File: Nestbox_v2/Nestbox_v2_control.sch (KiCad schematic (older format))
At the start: 28 parts, among them CON301 Micro_SD_Card, P301 RX/TX, P302 TST/RST, P303 DEBUG_3V3, SW301 SMD-BUTTON_2P-3.0X2.5X1.2+0.4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, U301 MSP430FR5969, Y301 Crystal

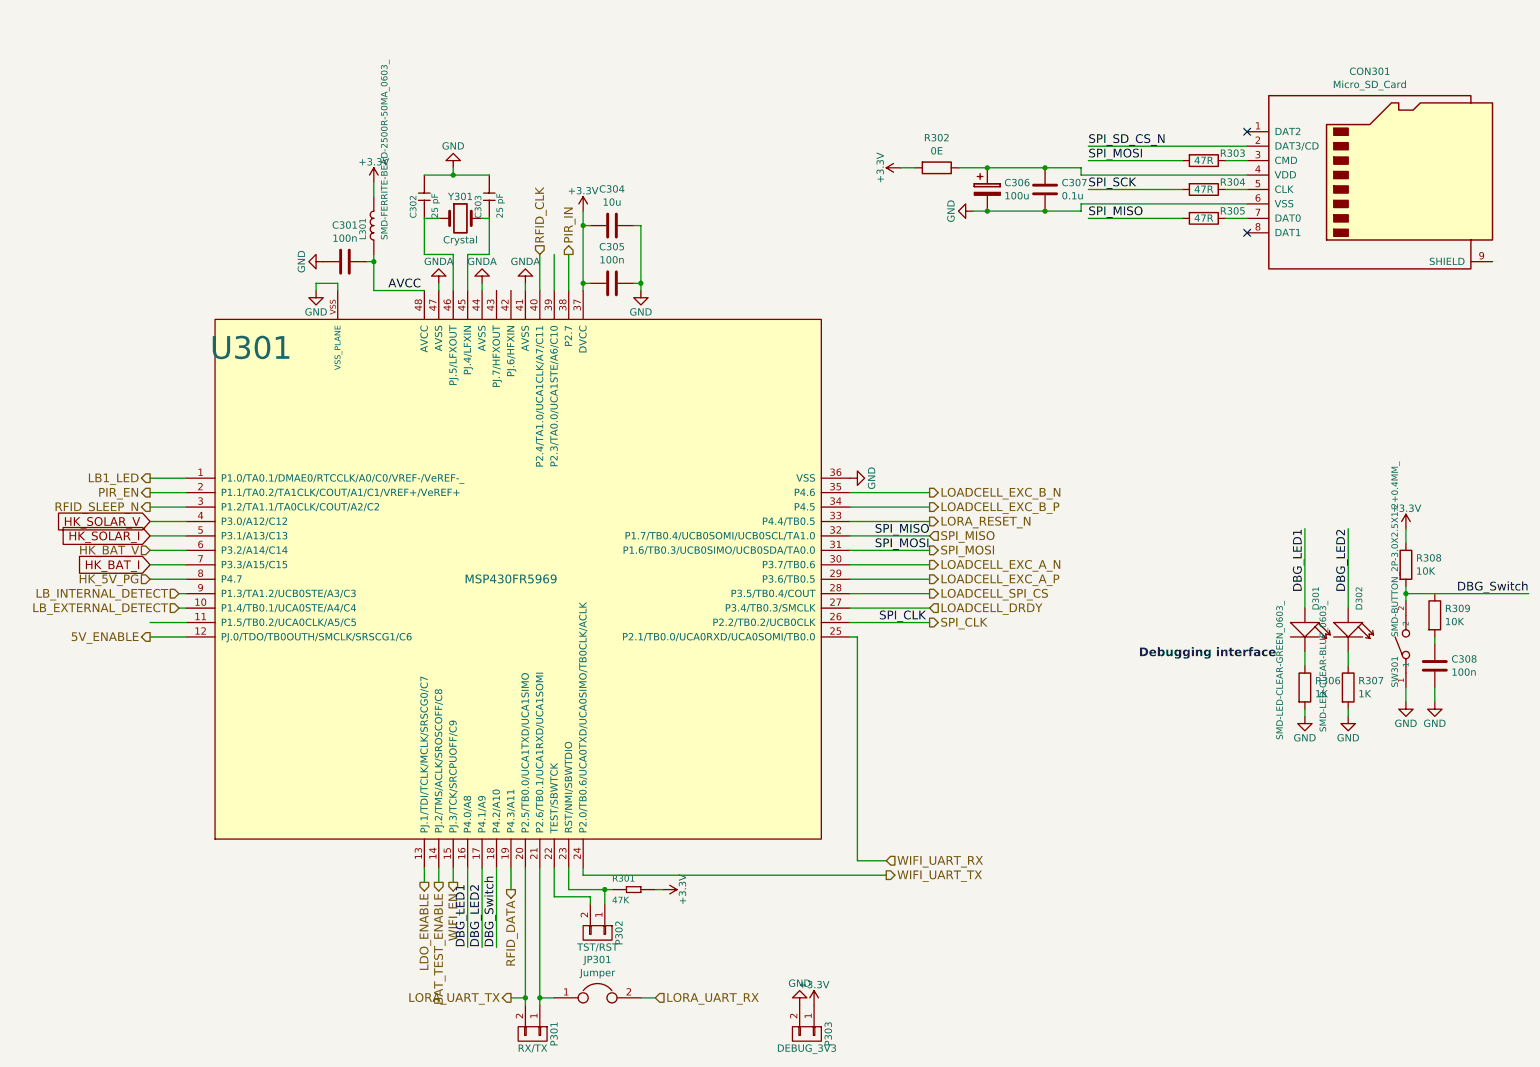
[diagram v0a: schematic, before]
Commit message: all footprints assigned except mosfets; final connectors and their locatino, started component placement
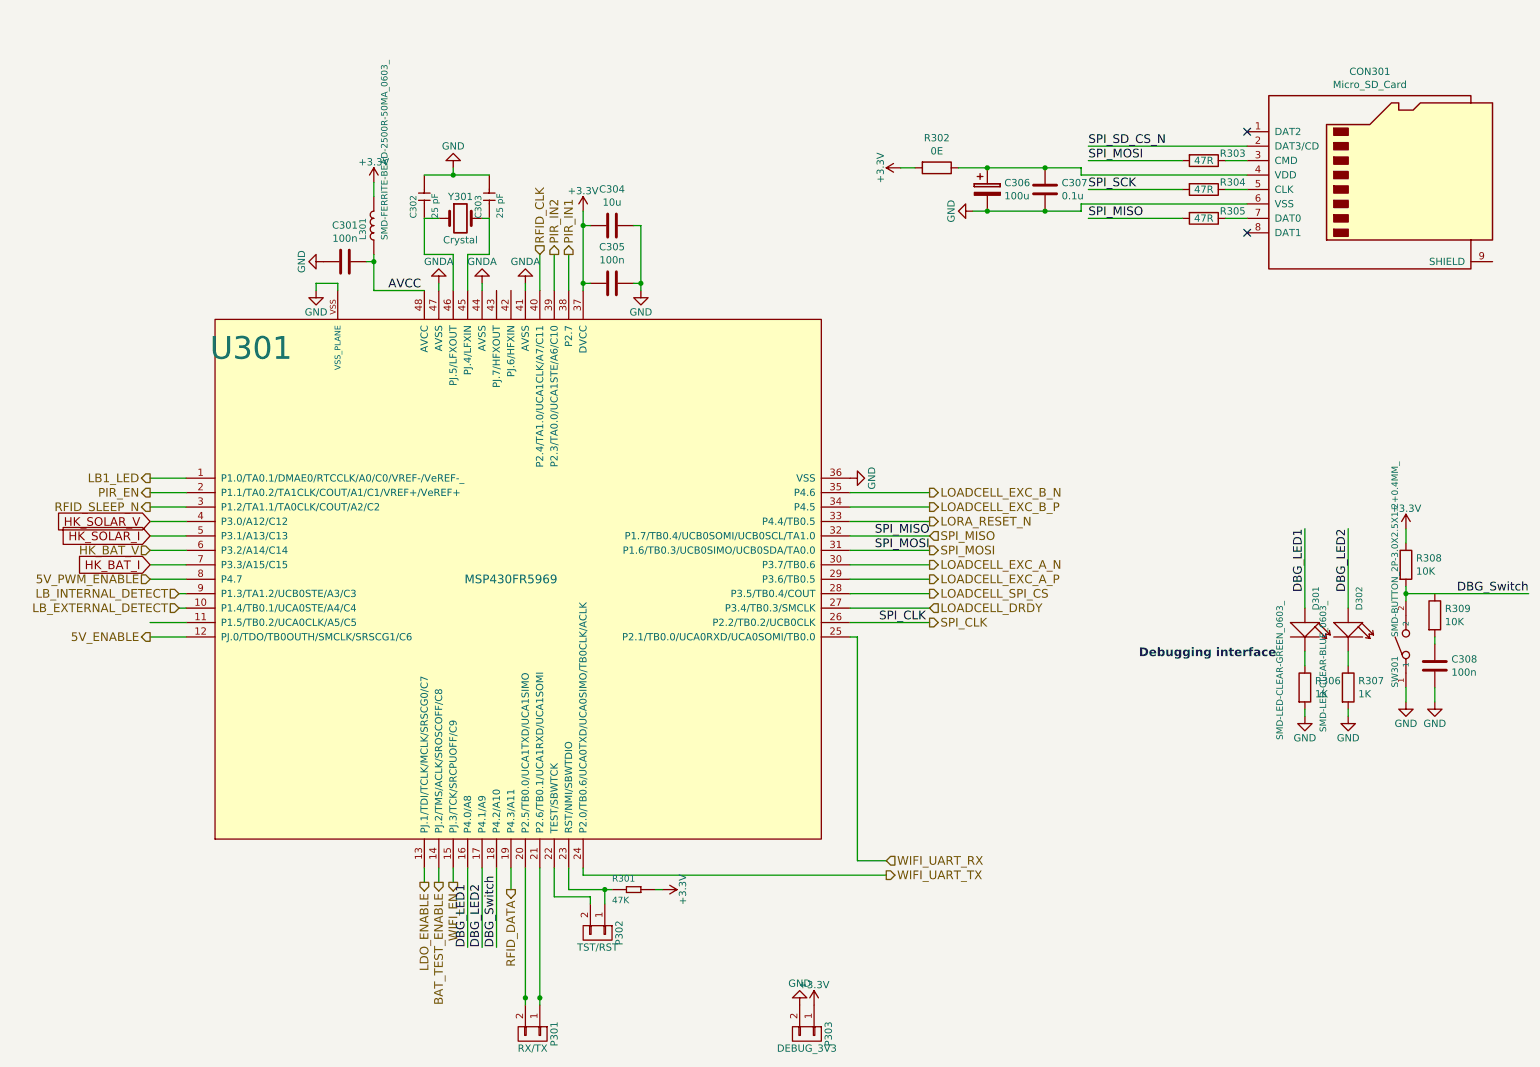
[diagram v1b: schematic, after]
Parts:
- removed JP301: Jumper, Pin_Headers:Pin_Header_Straight_1x02, symbol Jumper
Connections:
- net PIR_IN2: now reaches U301.39 (P2.3/TA0.0/UCA1STE/A6/C10)
- net HK_5V_PG renamed 5V_PWM_ENABLE
- net LORA_UART_TX: no longer names the net of P301.2 (P2), U301.20 (P2.5/TB0.0/UCA1TXD/UCA1SIMO)
- net PIR_IN renamed PIR_IN1
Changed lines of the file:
@@
 EESchema Schematic File Version 2
-LIBS:Nestbox_v2-rescue
-LIBS:Octanis3
 LIBS:power
 LIBS:device
-LIBS:switches
-LIBS:relays
-LIBS:motors
 LIBS:transistors
 LIBS:conn
@@
 LIBS:contrib
 LIBS:valves
-LIBS:SeeedOPL-Capacitor-2016
-LIBS:SeeedOPL-Connector-2016
-LIBS:SeeedOPL-Crystal Oscillator-2016
-LIBS:SeeedOPL-Diode-2016
-LIBS:SeeedOPL-Display-2016
-LIBS:SeeedOPL-Fuse-2016
-LIBS:SeeedOPL-IC-2016
-LIBS:SeeedOPL-Inductor-2016
-LIBS:SeeedOPL-LED-2016
-LIBS:SeeedOPL-Relay-2016
-LIBS:SeeedOPL-Resistor-2016
-LIBS:SeeedOPL-Sensor-2016
-LIBS:SeeedOPL-Switch-2016
-LIBS:SeeedOPL-Transistor-2016
+LIBS:Octanis3
 LIBS:Nestbox_v2-cache
 EELAYER 25 0
@@
 $EndComp
 $Comp
-L GND #PWR313
+L GND #PWR022
 U 1 1 586416A7
 P 6150 3750
-F 0 "#PWR313" H 6150 3500 50  0001 C CNN
+F 0 "#PWR022" H 6150 3500 50  0001 C CNN
 F 1 "GND" H 6150 3600 50  0000 C CNN
 F 2 "" H 6150 3750 50  0000 C CNN
@@
 $EndComp
 $Comp
-L +3.3V #PWR308
+L +3.3V #PWR023
 U 1 1 586418DC
 P 4300 1900
-F 0 "#PWR308" H 4300 1750 50  0001 C CNN
+F 0 "#PWR023" H 4300 1750 50  0001 C CNN
 F 1 "+3.3V" H 4300 2040 50  0000 C CNN
 F 2 "" H 4300 1900 50  0000 C CNN
@@
 $EndComp
 $Comp
-L GND #PWR302
+L GND #PWR024
 U 1 1 58641ADD
 P 2500 2250
-F 0 "#PWR302" H 2500 2000 50  0001 C CNN
+F 0 "#PWR024" H 2500 2000 50  0001 C CNN
 F 1 "GND" H 2500 2100 50  0000 C CNN
 F 2 "" H 2500 2250 50  0000 C CNN
@@
 $EndComp
 $Comp
-L +3.3V #PWR303
+L +3.3V #PWR025
 U 1 1 58641B00
 P 2850 1700
-F 0 "#PWR303" H 2850 1550 50  0001 C CNN
+F 0 "#PWR025" H 2850 1550 50  0001 C CNN
 F 1 "+3.3V" H 2850 1840 50  0000 C CNN
 F 2 "" H 2850 1700 50  0000 C CNN
@@
 $EndComp
 $Comp
-L GND #PWR309
+L GND #PWR026
 U 1 1 58652F3A
 P 4700 2450
-F 0 "#PWR309" H 4700 2200 50  0001 C CNN
+F 0 "#PWR026" H 4700 2200 50  0001 C CNN
 F 1 "GND" H 4700 2300 50  0000 C CNN
 F 2 "" H 4700 2450 50  0000 C CNN
@@
 $EndComp
 $Comp
-L GND #PWR305
+L GND #PWR027
 U 1 1 5865358A
 P 3400 1600
-F 0 "#PWR305" H 3400 1350 50  0001 C CNN
+F 0 "#PWR027" H 3400 1350 50  0001 C CNN
 F 1 "GND" H 3400 1450 50  0000 C CNN
 F 2 "" H 3400 1600 50  0000 C CNN
@@
 $EndComp
 $Comp
-L GNDA #PWR304
+L GNDA #PWR028
 U 1 1 587B6902
 P 3300 2400
-F 0 "#PWR304" H 3300 2150 50  0001 C CNN
+F 0 "#PWR028" H 3300 2150 50  0001 C CNN
 F 1 "GNDA" H 3300 2250 50  0000 C CNN
 F 2 "" H 3300 2400 50  0000 C CNN
@@
 $EndComp
 $Comp
-L GNDA #PWR306
+L GNDA #PWR029
 U 1 1 587B69F1
 P 3600 2400
-F 0 "#PWR306" H 3600 2150 50  0001 C CNN
+F 0 "#PWR029" H 3600 2150 50  0001 C CNN
 F 1 "GNDA" H 3600 2250 50  0000 C CNN
 F 2 "" H 3600 2400 50  0000 C CNN
@@
 $EndComp
 $Comp
-L GNDA #PWR307
+L GNDA #PWR030
 U 1 1 587B6A2F
 P 3900 2400
-F 0 "#PWR307" H 3900 2150 50  0001 C CNN
+F 0 "#PWR030" H 3900 2150 50  0001 C CNN
 F 1 "GNDA" H 3900 2250 50  0000 C CNN
 F 2 "" H 3900 2400 50  0000 C CNN
@@
 $EndComp
 $Comp
-L GND #PWR319
+L GND #PWR031
 U 1 1 587B96DD
 P 10000 5300
-F 0 "#PWR319" H 10000 5050 50  0001 C CNN
+F 0 "#PWR031" H 10000 5050 50  0001 C CNN
 F 1 "GND" H 10000 5150 50  0000 C CNN
 F 2 "" H 10000 5300 50  0000 C CNN
@@
 $EndComp
 $Comp
-L +3.3V #PWR318
+L +3.3V #PWR032
 U 1 1 587B9736
 P 10000 4100
-F 0 "#PWR318" H 10000 3950 50  0001 C CNN
+F 0 "#PWR032" H 10000 3950 50  0001 C CNN
 F 1 "+3.3V" H 10000 4240 50  0000 C CNN
 F 2 "" H 10000 4100 50  0000 C CNN
@@
 $EndComp
 $Comp
-L GND #PWR317
+L GND #PWR033
 U 1 1 587B97E4
 P 9600 5400
-F 0 "#PWR317" H 9600 5150 50  0001 C CNN
+F 0 "#PWR033" H 9600 5150 50  0001 C CNN
 F 1 "GND" H 9600 5250 50  0000 C CNN
 F 2 "" H 9600 5400 50  0000 C CNN
@@
 $EndComp
 $Comp
-L GND #PWR316
+L GND #PWR034
 U 1 1 587B9834
 P 9300 5400
-F 0 "#PWR316" H 9300 5150 50  0001 C CNN
+F 0 "#PWR034" H 9300 5150 50  0001 C CNN
 F 1 "GND" H 9300 5250 50  0000 C CNN
 F 2 "" H 9300 5400 50  0000 C CNN
@@
 	9300 4950 9300 5050
 $Comp
-L GND #PWR301
+L GND #PWR035
 U 1 1 587D2523
 P 2450 2450
-F 0 "#PWR301" H 2450 2200 50  0001 C CNN
+F 0 "#PWR035" H 2450 2200 50  0001 C CNN
 F 1 "GND" H 2450 2300 50  0000 C CNN
 F 2 "" H 2450 2450 50  0000 C CNN
@@
 	4350 6650 4350 6700
 $Comp
-L +3.3V #PWR310
+L +3.3V #PWR036
 U 1 1 58BC4BB7
 P 4850 6600
-F 0 "#PWR310" H 4850 6450 50  0001 C CNN
+F 0 "#PWR036" H 4850 6450 50  0001 C CNN
 F 1 "+3.3V" H 4850 6740 50  0000 C CNN
 F 2 "" H 4850 6600 50  0000 C CNN
@@
 	10200 4850 10200 4900
 $Comp
-L GND #PWR320
+L GND #PWR037
 U 1 1 58BF19D6
 P 10200 5300
-F 0 "#PWR320" H 10200 5050 50  0001 C CNN
+F 0 "#PWR037" H 10200 5050 50  0001 C CNN
 F 1 "GND" H 10200 5150 50  0000 C CNN
 F 2 "" H 10200 5300 50  0000 C CNN
@@
 SPI_MOSI
 $Comp
-L +3.3V #PWR314
+L +3.3V #PWR038
 U 1 1 59FCECA7
 P 6500 1600
-F 0 "#PWR314" H 6500 1450 50  0001 C CNN
+F 0 "#PWR038" H 6500 1450 50  0001 C CNN
 F 1 "+3.3V" H 6500 1740 50  0000 C CNN
 F 2 "" H 6500 1600 50  0000 C CNN
@@
 $EndComp
 $Comp
-L GND #PWR315
+L GND #PWR039
 U 1 1 59FCED84
 P 7000 1900
-F 0 "#PWR315" H 7000 1650 50  0001 C CNN
+F 0 "#PWR039" H 7000 1650 50  0001 C CNN
 F 1 "GND" H 7000 1750 50  0000 C CNN
 F 2 "" H 7000 1900 50  0000 C CNN
@@
 Wire Wire Line
 	1550 4050 1300 4050
-Wire Wire Line
-	4800 7350 4700 7350
-$Comp
-L Jumper JP301
-U 1 1 5A03190F
-P 4400 7350
-F 0 "JP301" H 4400 7614 50  0000 C CNN
-F 1 "Jumper" H 4400 7523 50  0000 C CNN
-F 2 "Pin_Headers:Pin_Header_Straight_1x02" H 4400 7350 50  0001 C CNN
-F 3 "" H 4400 7350 50  0001 C CNN
-	1    4400 7350
-	1    0    0    -1
-$EndComp
 Connection ~ 4000 7350
-Wire Wire Line
-	4100 7350 4000 7350
 Connection ~ 3900 7350
-Wire Wire Line
-	3800 7350 3900 7350
 Wire Wire Line
 	4000 6450 4000 7400
@@
 	4000 2200 4000 2450
 Text HLabel 1300 4450 0    60   Input ~ 0
-HK_5V_PG
+5V_PWM_ENABLE
 Text HLabel 1300 4250 0    60   Input ~ 0
 HK_BAT_V
@@
 Text HLabel 3200 6550 3    60   Output ~ 0
 LDO_ENABLE
-Text HLabel 3800 7350 0    60   Output ~ 0
-LORA_UART_TX
-Text HLabel 4800 7350 2    60   Input ~ 0
-LORA_UART_RX
 Text HLabel 6400 6400 2    60   Input ~ 0
 WIFI_UART_RX
@@
 HK_BAT_I
 Text HLabel 4200 2200 1    60   Output ~ 0
-PIR_IN
+PIR_IN1
 Wire Wire Line
 	4200 2200 4200 2450
@@
 $EndComp
 $Comp
-L +3.3V #PWR312
+L +3.3V #PWR040
 U 1 1 5B0C49AB
 P 5900 7400
-F 0 "#PWR312" H 5900 7250 50  0001 C CNN
+F 0 "#PWR040" H 5900 7250 50  0001 C CNN
 F 1 "+3.3V" H 5900 7540 50  0000 C CNN
 F 2 "" H 5900 7400 50  0000 C CNN
@@
 $EndComp
 $Comp
-L GND #PWR311
+L GND #PWR041
 U 1 1 5B0C4B76
 P 5800 7400
-F 0 "#PWR311" H 5800 7150 50  0001 C CNN
+F 0 "#PWR041" H 5800 7150 50  0001 C CNN
 F 1 "GND" H 5800 7250 50  0000 C CNN
 F 2 "" H 5800 7400 50  0000 C CNN
@@
 	-1   0    0    1
 $EndComp
+Text HLabel 4100 2200 1    60   Output ~ 0
+PIR_IN2
 $EndSCHEMATC

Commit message: finished component placement
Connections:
- net DBG_Switch: now also R309.1
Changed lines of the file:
@@
 Text HLabel 4100 2200 1    60   Output ~ 0
 PIR_IN2
+Connection ~ 10200 4550
 $EndSCHEMATC

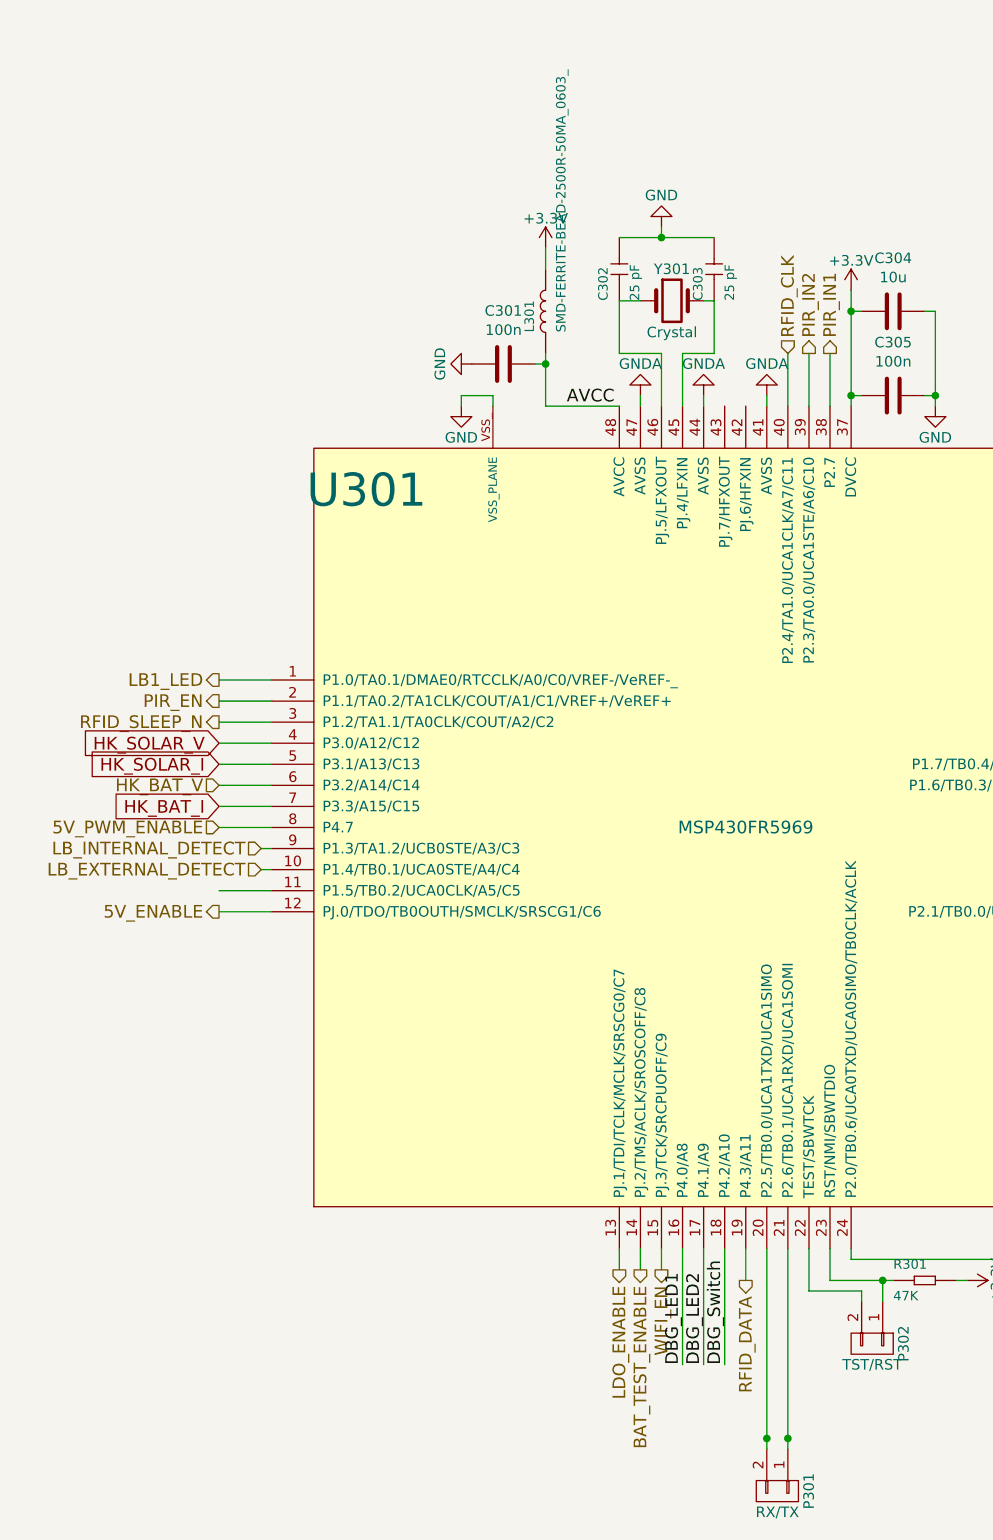
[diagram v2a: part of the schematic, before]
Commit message: routed all tracks except ground plane
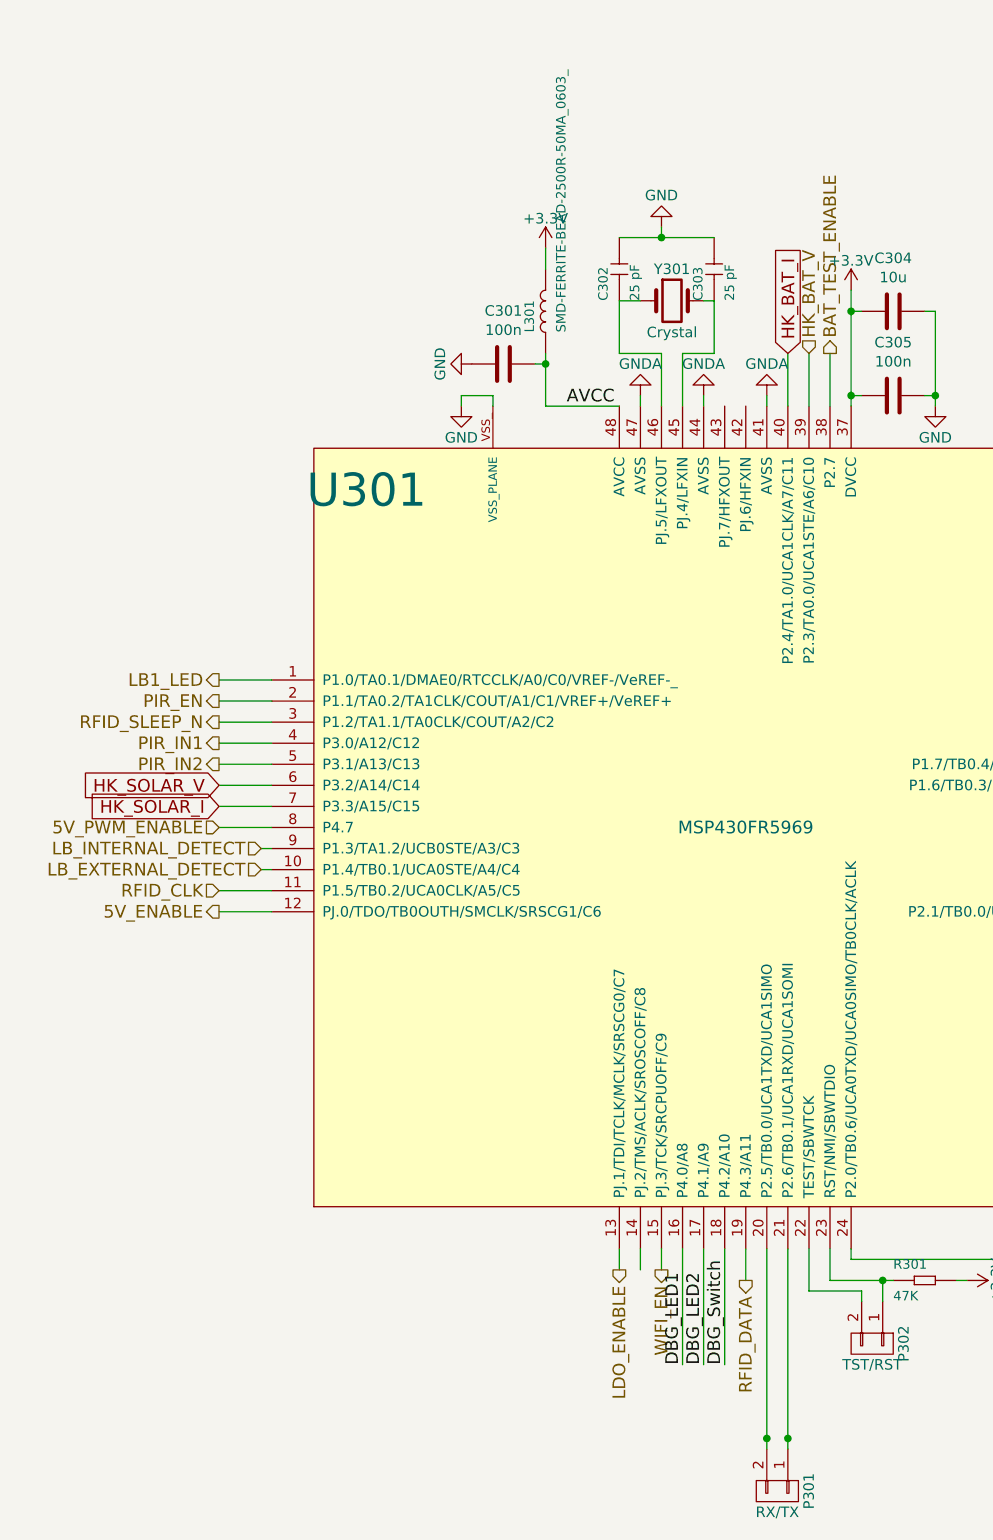
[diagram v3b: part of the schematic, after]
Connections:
- net BAT_TEST_ENABLE: now also U301.38 (P2.7); no longer U301.14 (PJ.2/TMS/ACLK/SROSCOFF/C8)
- net HK_BAT_I: now also U301.40 (P2.4/TA1.0/UCA1CLK/A7/C11); no longer U301.7 (P3.3/A15/C15)
- net HK_BAT_V: now also U301.39 (P2.3/TA0.0/UCA1STE/A6/C10); no longer U301.6 (P3.2/A14/C14)
- net HK_SOLAR_I: now also U301.7 (P3.3/A15/C15); no longer U301.5 (P3.1/A13/C13)
- net HK_SOLAR_V: now also U301.6 (P3.2/A14/C14); no longer U301.4 (P3.0/A12/C12)
- net PIR_IN1: now also U301.4 (P3.0/A12/C12); no longer U301.38 (P2.7)
- net PIR_IN2: now also U301.5 (P3.1/A13/C13); no longer U301.39 (P2.3/TA0.0/UCA1STE/A6/C10)
- net RFID_CLK: now also U301.11 (P1.5/TB0.2/UCA0CLK/A5/C5); no longer U301.40 (P2.4/TA1.0/UCA1CLK/A7/C11)
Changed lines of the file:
@@
 Wire Wire Line
 	1300 4750 1550 4750
-Text GLabel 1300 4050 0    60   Input ~ 0
+Text GLabel 1300 4250 0    60   Input ~ 0
 HK_SOLAR_V
 Wire Wire Line
@@
 	0    1    1    0
 $EndComp
-Text GLabel 1300 4150 0    60   Input ~ 0
+Text GLabel 1300 4350 0    60   Input ~ 0
 HK_SOLAR_I
 Wire Wire Line
@@
 Text HLabel 1300 3950 0    60   Output ~ 0
 RFID_SLEEP_N
-Text HLabel 4000 2200 1    60   Input ~ 0
+Text HLabel 1300 4750 0    60   Input ~ 0
 RFID_CLK
 Wire Wire Line
@@
 Text HLabel 1300 4450 0    60   Input ~ 0
 5V_PWM_ENABLE
-Text HLabel 1300 4250 0    60   Input ~ 0
+Text HLabel 4100 2200 1    60   Input ~ 0
 HK_BAT_V
 Text HLabel 1300 4850 0    60   Output ~ 0
@@
 Text HLabel 6700 3850 2    60   Output ~ 0
 LOADCELL_EXC_B_N
-Text HLabel 3300 6550 3    60   Output ~ 0
+Text HLabel 4200 2200 1    60   Output ~ 0
 BAT_TEST_ENABLE
 Wire Wire Line
@@
 Text HLabel 1300 3850 0    60   Output ~ 0
 PIR_EN
-Text GLabel 1300 4350 0    60   Input ~ 0
+Text GLabel 4000 2200 1    60   Input ~ 0
 HK_BAT_I
-Text HLabel 4200 2200 1    60   Output ~ 0
+Text HLabel 1300 4050 0    60   Output ~ 0
 PIR_IN1
 Wire Wire Line
@@
 	-1   0    0    1
 $EndComp
-Text HLabel 4100 2200 1    60   Output ~ 0
+Text HLabel 1300 4150 0    60   Output ~ 0
 PIR_IN2
 Connection ~ 10200 4550
